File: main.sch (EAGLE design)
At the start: 27 parts, among them IC1 FT232RL, U1 ATMEGA328P_TQFP, Y3 16MHz

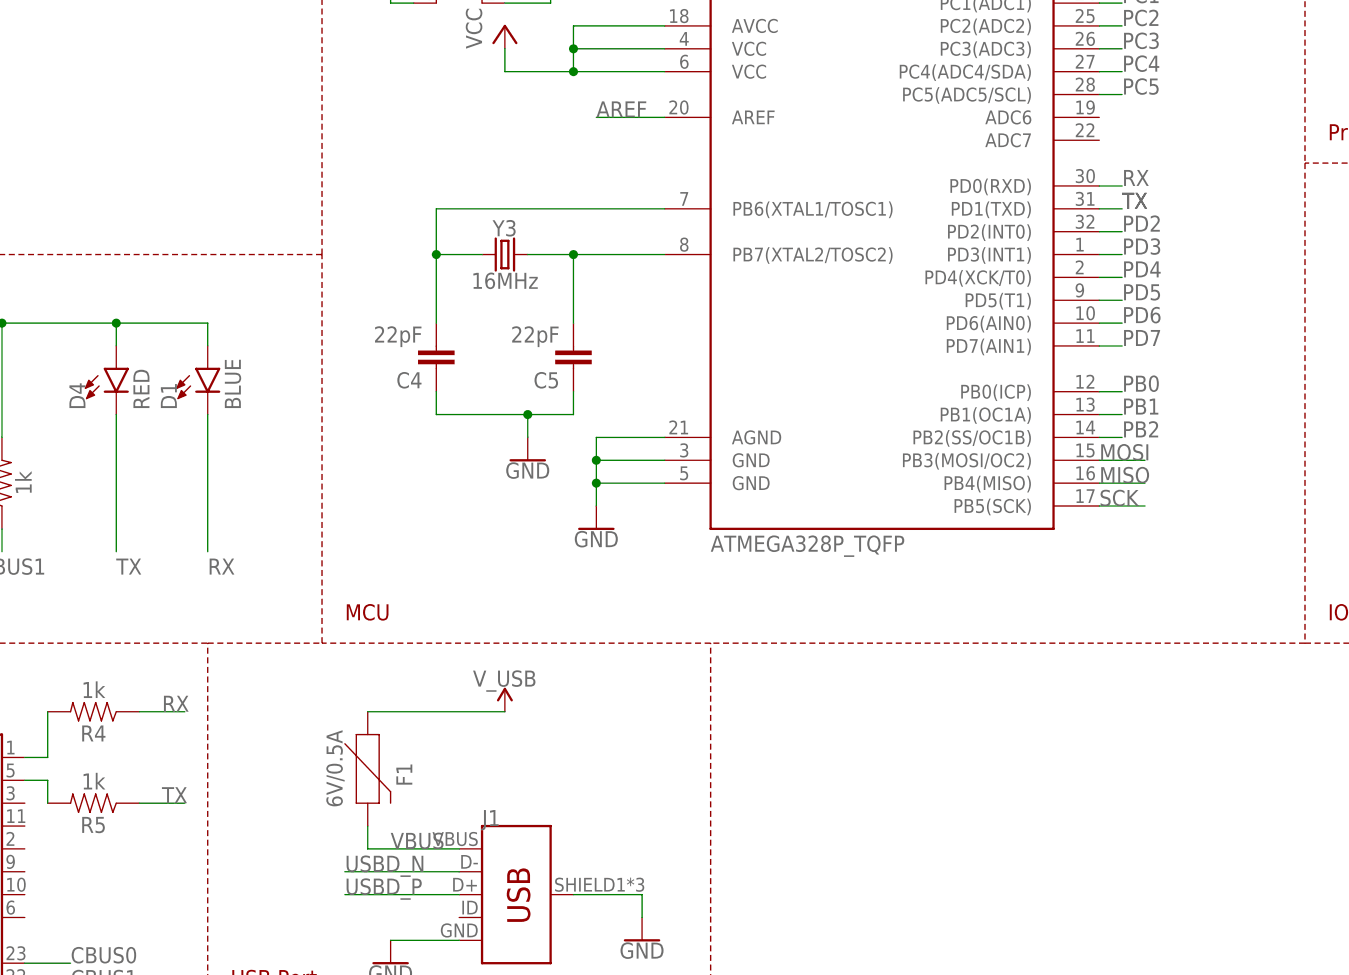
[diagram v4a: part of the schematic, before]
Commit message: ROutes RX and TX
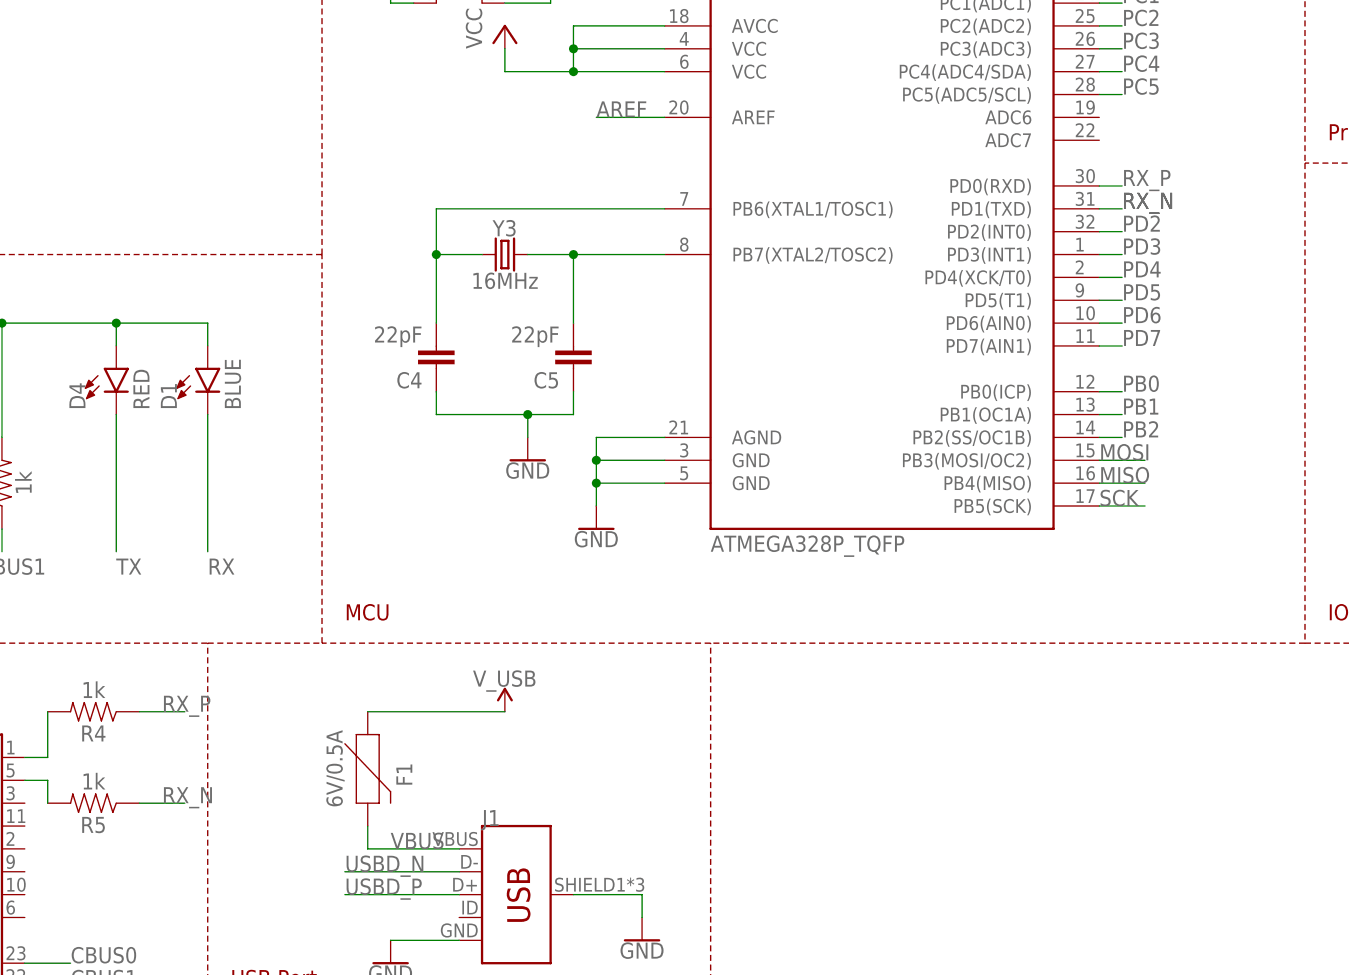
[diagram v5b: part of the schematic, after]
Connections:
- new net RX_1_N: IC1.RXD, R5.2
- new net RX_1_P: IC1.TXD, R4.2
- new net RX_N: R5.1, U1.PD1(TXD)
- new net RX_P: R4.1, U1.PD0(RXD)
- net RX: no longer IC1.RXD, IC1.TXD, R4.1, R4.2, R5.2, U1.PD0(RXD)
- net TX: no longer R5.1, U1.PD1(TXD)
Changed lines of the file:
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@@
-</segment>
-<segment>
-<wire x1="129.54" y1="104.14" x2="132.08" y2="104.14" width="0.1524" layer="91"/>
-<label x="132.08" y="104.14" size="1.778" layer="95"/>
-<label x="132.08" y="104.14" size="1.778" layer="95"/>
-<pinref part="U1" gate="U$1" pin="PD1(TXD)"/>
 </segment>
 <segment>
@@
 </segment>
 <segment>
-<wire x1="22.86" y1="38.1" x2="27.94" y2="38.1" width="0.1524" layer="91"/>
-<label x="25.4" y="38.1" size="1.778" layer="95"/>
-<pinref part="R5" gate="G$1" pin="1"/>
-</segment>
-<segment>
 <label x="20.32" y="63.5" size="1.778" layer="95"/>
 <pinref part="D4" gate="G$1" pin="C"/>
@@
 </segment>
 <segment>
-<wire x1="129.54" y1="106.68" x2="132.08" y2="106.68" width="0.1524" layer="91"/>
-<label x="132.08" y="106.68" size="1.778" layer="95"/>
-<pinref part="U1" gate="U$1" pin="PD0(RXD)"/>
-</segment>
-<segment>
 <pinref part="JP5" gate="A" pin="5"/>
 <wire x1="195.58" y1="81.28" x2="180.34" y2="81.28" width="0.1524" layer="91"/>
@@
 </segment>
 <segment>
-<wire x1="22.86" y1="48.26" x2="27.94" y2="48.26" width="0.1524" layer="91"/>
-<label x="25.4" y="48.26" size="1.778" layer="95"/>
-<pinref part="R4" gate="G$1" pin="1"/>
-</segment>
-<segment>
-<pinref part="IC1" gate="1" pin="TXD"/>
-<wire x1="10.16" y1="43.18" x2="12.7" y2="43.18" width="0.1524" layer="91"/>
-<wire x1="12.7" y1="43.18" x2="12.7" y2="48.26" width="0.1524" layer="91"/>
-<pinref part="R4" gate="G$1" pin="2"/>
-</segment>
-<segment>
 <label x="30.48" y="63.5" size="1.778" layer="95"/>
 <pinref part="D1" gate="G$1" pin="C"/>
 <wire x1="30.48" y1="66.04" x2="30.48" y2="81.28" width="0.1524" layer="91"/>
-</segment>
-<segment>
-<pinref part="IC1" gate="1" pin="RXD"/>
-<pinref part="R5" gate="G$1" pin="2"/>
-<wire x1="10.16" y1="40.64" x2="12.7" y2="40.64" width="0.1524" layer="91"/>
-<wire x1="12.7" y1="40.64" x2="12.7" y2="38.1" width="0.1524" layer="91"/>
 </segment>
 </net>
@@
 </segment>
 </net>
+<net name="RX_P" class="0">
+<segment>
+<wire x1="22.86" y1="48.26" x2="27.94" y2="48.26" width="0.1524" layer="91"/>
+<label x="25.4" y="48.26" size="1.778" layer="95"/>
+<pinref part="R4" gate="G$1" pin="1"/>
+</segment>
+<segment>
+<wire x1="129.54" y1="106.68" x2="132.08" y2="106.68" width="0.1524" layer="91"/>
+<label x="132.08" y="106.68" size="1.778" layer="95"/>
+<pinref part="U1" gate="U$1" pin="PD0(RXD)"/>
+</segment>
+</net>
+<net name="RX_N" class="0">
+<segment>
+<wire x1="22.86" y1="38.1" x2="27.94" y2="38.1" width="0.1524" layer="91"/>
+<label x="25.4" y="38.1" size="1.778" layer="95"/>
+<pinref part="R5" gate="G$1" pin="1"/>
+</segment>
+<segment>
+<wire x1="129.54" y1="104.14" x2="132.08" y2="104.14" width="0.1524" layer="91"/>
+<label x="132.08" y="104.14" size="1.778" layer="95"/>
+<label x="132.08" y="104.14" size="1.778" layer="95"/>
+<pinref part="U1" gate="U$1" pin="PD1(TXD)"/>
+</segment>
+</net>
+<net name="RX_1_P" class="0">
+<segment>
+<pinref part="IC1" gate="1" pin="TXD"/>
+<wire x1="10.16" y1="43.18" x2="12.7" y2="43.18" width="0.1524" layer="91"/>
+<wire x1="12.7" y1="43.18" x2="12.7" y2="48.26" width="0.1524" layer="91"/>
+<pinref part="R4" gate="G$1" pin="2"/>
+</segment>
+</net>
+<net name="RX_1_N" class="0">
+<segment>
+<pinref part="IC1" gate="1" pin="RXD"/>
+<pinref part="R5" gate="G$1" pin="2"/>
+<wire x1="10.16" y1="40.64" x2="12.7" y2="40.64" width="0.1524" layer="91"/>
+<wire x1="12.7" y1="40.64" x2="12.7" y2="38.1" width="0.1524" layer="91"/>
+</segment>
+</net>
